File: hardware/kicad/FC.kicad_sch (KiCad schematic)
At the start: 0 parts

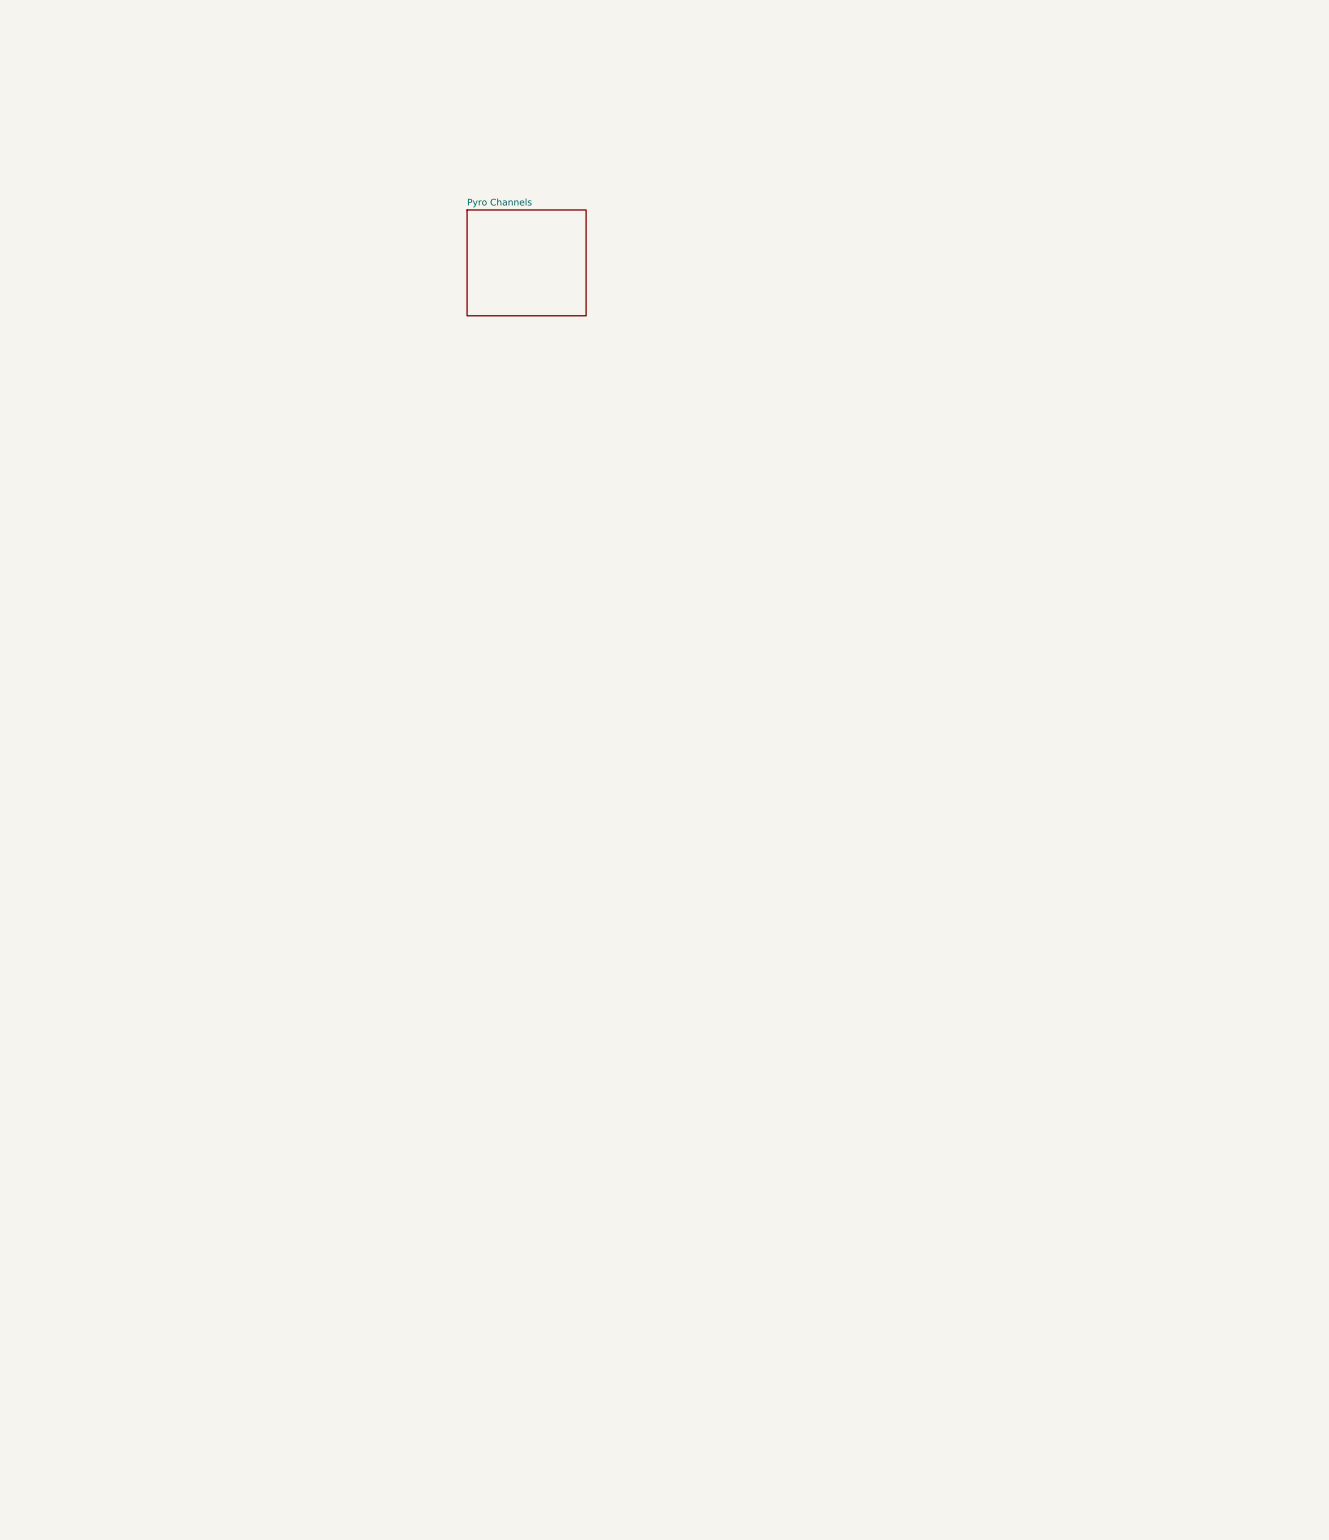
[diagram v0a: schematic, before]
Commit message: created schematic files
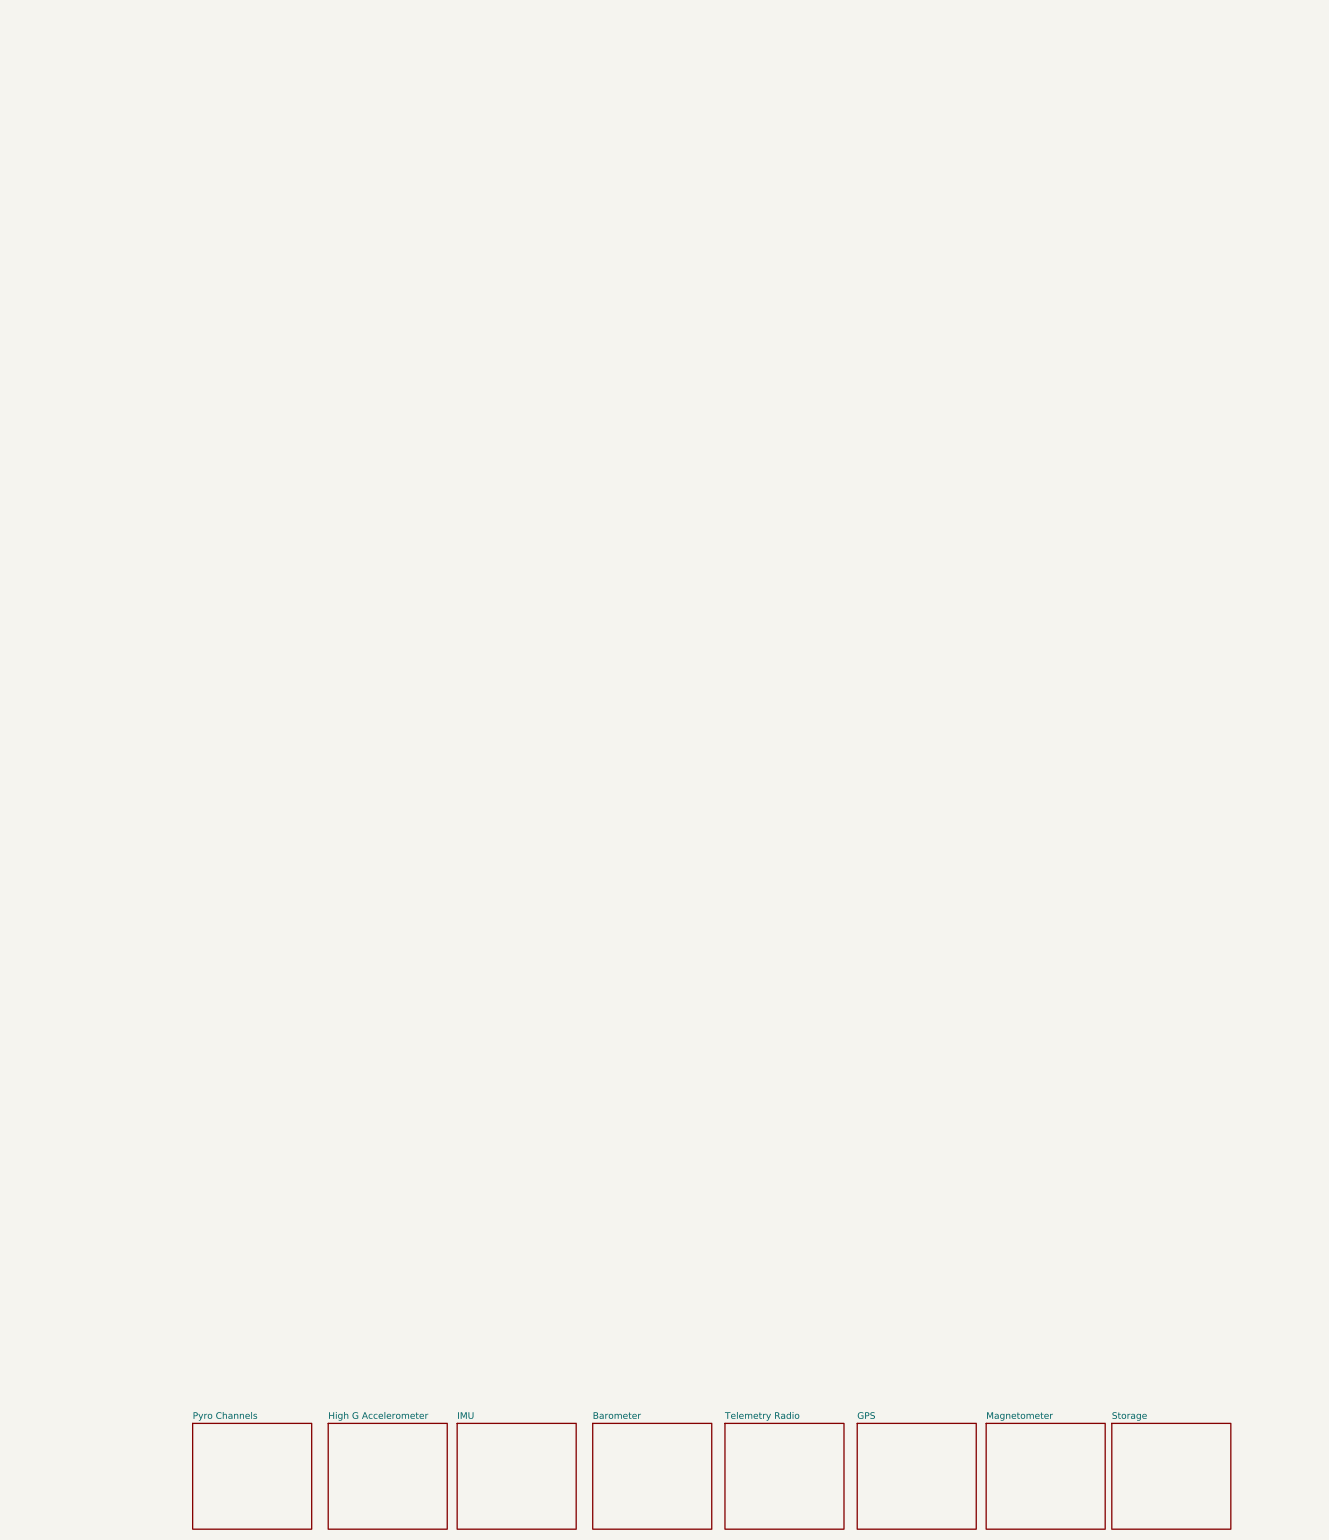
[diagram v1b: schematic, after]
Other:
- added sheet Barometer (hierarchical_sheets/ms5611.kicad_sch)
- added sheet GPS (hierarchical_sheets/m10s.kicad_sch)
- added sheet High G Accelerometer (hierarchical_sheets/kx134-1211.kicad_sch)
- added sheet IMU (hierarchical_sheets/bmi-270.kicad_sch)
- added sheet Magnetometer (hierarchical_sheets/bmm-350.kicad_sch)
- added sheet Storage (hierarchical_sheets/mb85rs2mtapnf.kicad_sch)
- added sheet Telemetry Radio (hierarchical_sheets/ra-01sh.kicad_sch)
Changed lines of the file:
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@@
 (kicad_sch (version 20230121) (generator eeschema)
   (paper "A4")
-  (sheet (at 100.965 70.485) (size 22.86 20.32) (fields_autoplaced)
+  (sheet (at 125.095 303.53) (size 22.86 20.32) (fields_autoplaced)
     (stroke (width 0.1524) (type solid))
     (fill (color 255 255 194 1.0000))
-    (property "Sheetname" "Pyro Channels" (at 100.965 69.7734 0)
+    (property "Sheetname" "Barometer" (at 125.095 302.8184 0)
       (effects (font (size 1.27 1.27)) (justify left bottom))
     )
-    (property "Sheetfile" "hierarchical_sheets/pyro_channel.kicad_sch" (at 100.965 91.3896 0)
+    (property "Sheetfile" "hierarchical_sheets/ms5611.kicad_sch" (at 125.095 324.4346 0)
+      (effects (font (size 1.27 1.27)) (justify left top) hide)
+    )
+    (instances
+      (project "FC"
+        (path "/54cce219-8b98-4e71-96c4-f9ee784aa3bc" (page "5"))
+      )
+    )
+  )
+  (sheet (at 48.26 303.53) (size 22.86 20.32) (fields_autoplaced)
+    (stroke (width 0.1524) (type solid))
+    (fill (color 255 255 194 1.0000))
+    (property "Sheetname" "Pyro Channels" (at 48.26 302.8184 0)
+      (effects (font (size 1.27 1.27)) (justify left bottom))
+    )
+    (property "Sheetfile" "hierarchical_sheets/pyro_channel.kicad_sch" (at 48.26 324.4346 0)
       (effects (font (size 1.27 1.27)) (justify left top) hide)
     )
@@
       )
     )
+  )
+  (sheet (at 150.495 303.53) (size 22.86 20.32) (fields_autoplaced)
+    (stroke (width 0.1524) (type solid))
+    (fill (color 255 255 194 1.0000))
+    (property "Sheetname" "Telemetry Radio" (at 150.495 302.8184 0)
+      (effects (font (size 1.27 1.27)) (justify left bottom))
+    )
+    (property "Sheetfile" "hierarchical_sheets/ra-01sh.kicad_sch" (at 150.495 324.4346 0)
+      (effects (font (size 1.27 1.27)) (justify left top) hide)
+    )
+    (instances
+      (project "FC"
+        (path "/54cce219-8b98-4e71-96c4-f9ee784aa3bc" (page "6"))
+      )
+    )
+  )
+  (sheet (at 200.66 303.53) (size 22.86 20.32) (fields_autoplaced)
+    (stroke (width 0.1524) (type solid))
+    (fill (color 255 255 194 1.0000))
+    (property "Sheetname" "Magnetometer" (at 200.66 302.8184 0)
+      (effects (font (size 1.27 1.27)) (justify left bottom))
+    )
+    (property "Sheetfile" "hierarchical_sheets/bmm-350.kicad_sch" (at 200.66 324.4346 0)
+      (effects (font (size 1.27 1.27)) (justify left top) hide)
+    )
+    (instances
+      (project "FC"
+        (path "/54cce219-8b98-4e71-96c4-f9ee784aa3bc" (page "8"))
+      )
+    )
+  )
+  (sheet (at 99.06 303.53) (size 22.86 20.32) (fields_autoplaced)
+    (stroke (width 0.1524) (type solid))
+    (fill (color 255 255 194 1.0000))
+    (property "Sheetname" "IMU" (at 99.06 302.8184 0)
+      (effects (font (size 1.27 1.27)) (justify left bottom))
+    )
+    (property "Sheetfile" "hierarchical_sheets/bmi-270.kicad_sch" (at 99.06 324.4346 0)
+      (effects (font (size 1.27 1.27)) (justify left top) hide)
+    )
+    (instances
+      (project "FC"
+        (path "/54cce219-8b98-4e71-96c4-f9ee784aa3bc" (page "4"))
+      )
+    )
+  )
+  (sheet (at 74.295 303.53) (size 22.86 20.32) (fields_autoplaced)
+    (stroke (width 0.1524) (type solid))
+    (fill (color 255 255 194 1.0000))
+    (property "Sheetname" "High G Accelerometer" (at 74.295 302.8184 0)
+      (effects (font (size 1.27 1.27)) (justify left bottom))
+    )
+    (property "Sheetfile" "hierarchical_sheets/kx134-1211.kicad_sch" (at 74.295 324.4346 0)
+      (effects (font (size 1.27 1.27)) (justify left top) hide)
+    )
+    (instances
+      (project "FC"
+        (path "/54cce219-8b98-4e71-96c4-f9ee784aa3bc" (page "3"))
+      )
+    )
+  )
+  (sheet (at 224.79 303.53) (size 22.86 20.32) (fields_autoplaced)
+    (stroke (width 0.1524) (type solid))
+    (fill (color 255 255 194 1.0000))
+    (property "Sheetname" "Storage" (at 224.79 302.8184 0)
+      (effects (font (size 1.27 1.27)) (justify left bottom))
+    )
+    (property "Sheetfile" "hierarchical_sheets/mb85rs2mtapnf.kicad_sch" (at 224.79 324.4346 0)
+      (effects (font (size 1.27 1.27)) (justify left top) hide)
+    )
+    (instances
+      (project "FC"
+        (path "/54cce219-8b98-4e71-96c4-f9ee784aa3bc" (page "9"))
+      )
+    )
+  )
+  (sheet (at 175.895 303.53) (size 22.86 20.32) (fields_autoplaced)
+    (stroke (width 0.1524) (type solid))
+    (fill (color 255 255 194 1.0000))
+    (property "Sheetname" "GPS" (at 175.895 302.8184 0)
+      (effects (font (size 1.27 1.27)) (justify left bottom))
+    )
+    (property "Sheetfile" "hierarchical_sheets/m10s.kicad_sch" (at 175.895 324.4346 0)
+      (effects (font (size 1.27 1.27)) (justify left top) hide)
+    )
+    (instances
+      (project "FC"
+        (path "/54cce219-8b98-4e71-96c4-f9ee784aa3bc" (page "7"))
+      )
+    )
